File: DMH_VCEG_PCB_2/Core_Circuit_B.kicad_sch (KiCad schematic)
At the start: 103 parts, among them J24 Conn_01x06_PinHeader, J25 Conn_01x10_PinHeader, J26 Conn_01x10_PinHeader, Q17 BC558, Q18 BC558, Q19 BC548, Q20 BC548, Q21 MMBFJ113, Q22 MMBFJ113, Q23 BC548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

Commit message: Synced changes to PCB 2
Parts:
- removed Q21, Q22: MMBFJ113, Package_TO_SOT_THT:TO-92L_Inline, symbol Transistor_FET:MMBFJ113
- removed R108, R115, R116: 100k, Resistor_THT:R_Axial_DIN0207_L6.3mm_D2.5mm_P7.62mm_Horizontal, symbol Device:R_US
- added C75, C76: 100nF, Capacitor_THT:C_Rect_L7.0mm_W4.5mm_P5.00mm, symbol Device:C
- added Q21, Q22: BS170, Package_TO_SOT_THT:TO-92_Inline, symbol Transistor_FET:BS170
- added R19: 47k, Resistor_THT:R_Axial_DIN0207_L6.3mm_D2.5mm_P7.62mm_Horizontal, symbol Device:R_US
- added R199: 100R, Resistor_THT:R_Axial_DIN0207_L6.3mm_D2.5mm_P7.62mm_Horizontal, symbol Device:R_US
- added unit 4 of U13
- R129: value 100k -> 51k
- R131: value 100k -> 47k
- SW4: value DPDT_OnOn -> DPDT_OnOffOn; Function Long B -> Slow B
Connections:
- net -12V: no longer R138.1
- net GND: now also SW4.2 (B), SW4.5 (B), C75.1, C76.1, R19.1; no longer C61.1, C66.2, SW4.3 (C), SW4.6 (C)
- net InvGate: now also Q22.2 (G)
- net Max Level: now also R199.2; no longer U15.9 (-)
- net ProcGate: now also C62.1, D22.1 (K), D24.1 (K), J24.5 (Pin_5), R121.2, SW5.3 (C), U13.1, Q21.2 (G); no longer C64.2, D24.2 (A), R120.1, U11.1
- net at C61.2, C65.1, J25.6 (Pin_6)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: now also C76.2, Q21.1 (D), Q22.1 (D)
- net at C65.2: now also SW4.6 (C); no longer SW4.5 (B)
- net at Q20.1 (C): now also Q22.3 (S)
- net at R134.1, U11.8: now also U15.2 (-); no longer U15.3 (+)
- net at Q18.1 (C): now also Q21.3 (S)
- net at C66.1, C67.1, J25.7 (Pin_7)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: now also C75.2
- net at J24.4 (Pin_4), SW5.2 (B): now also D32.1 (K); no longer R131.1, U11.14
- net at D34.2 (A), U15.1: now also R138.2
- net Inv Sus State: now reaches U16.2, U16.4
- net at U16.10: now also U16.6; no longer D35.2 (A)
- net at U16.9: now also U13.8; no longer U13.4
- net at SW4.4 (A): now also C61.1
- net at SW4.1 (A): now also C66.2
- net at C67.2: now also SW4.3 (C); no longer SW4.2 (B)
- net at C71.2, R143.1: now also U13.9; no longer U16.6
- net Sus State renamed Sus_State
- new net: D32.2 (A), R131.1, U11.14
- new net: R19.2, R199.1, U15.9 (-)
- new net: C64.2, D24.2 (A), R120.1, U11.1
- new net: R138.1, R141.1, U15.3 (+)
- new net: D35.2 (A), U13.4
- no-connect marks 4 -> 2
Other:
- moved on the sheet: C61, C65, C66, C67, C69, C71, C72, D32, D34, D35, J24E, J26J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

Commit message: PCB 2 comp placement ongoing
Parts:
- C75, C76: footprint Capacitor_THT:C_Rect_L7.0mm_W4.5mm_P5.00mm -> Capacitor_THT:C_Disc_D4.3mm_W1.9mm_P5.00mm
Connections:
- net at C65.2: now also SW4.4 (A); no longer SW4.6 (C)
- net at C66.2: now also SW4.3 (C); no longer SW4.1 (A)
- net at C61.1: now also SW4.6 (C); no longer SW4.4 (A)
- net at C67.2: now also SW4.1 (A); no longer SW4.3 (C)
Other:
- moved on the sheet: C61, C65, C66, C67
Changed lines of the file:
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@@
 	(symbol
 		(lib_id "Device:C_Polarized")
-		(at 246.38 97.79 90)
+		(at 246.38 87.63 90)
 		(unit 1)
 		(exclude_from_sim no)
@@
 		(dnp no)
 		(property "Reference" "C65"
-			(at 245.618 91.186 90)
+			(at 245.618 81.026 90)
 			(effects
 				(font
@@
 		)
 		(property "Value" "10uF"
-			(at 245.618 93.726 90)
+			(at 245.618 83.566 90)
 			(effects
 				(font
@@
 		)
 		(property "Footprint" "Capacitor_THT:CP_Radial_D4.0mm_P1.50mm"
-			(at 250.19 96.8248 0)
+			(at 250.19 86.6648 0)
 			(effects
 				(font
@@
 		)
 		(property "Datasheet" "~"
-			(at 246.38 97.79 0)
+			(at 246.38 87.63 0)
 			(effects
 				(font
@@
 		)
 		(property "Description" "Polarized capacitor"
-			(at 246.38 97.79 0)
+			(at 246.38 87.63 0)
 			(effects
 				(font
@@
 		)
 		(property "Function" ""
-			(at 246.38 97.79 0)
+			(at 246.38 87.63 0)
 			(effects
 				(font
@@
 		)
 		(instances
-			(project "DMH_VCEG_PCB_1"
+			(project "DMH_VCEG_PCB_2"
 				(path "/58f4306d-5387-4983-bb08-41a2313fd315/8d22a13f-1d3b-4a1f-8b3f-baf42965c019"
 					(reference "C65")
@@
 		(exclude_from_sim no)
 		(in_bom yes)
-		(on_board yes)
+		(on_board no)
 		(dnp no)
 		(property "Reference" "R199"
@@
 		(exclude_from_sim no)
 		(in_bom yes)
-		(on_board yes)
+		(on_board no)
 		(dnp no)
 		(property "Reference" "R19"
@@
 			)
 		)
-		(property "Footprint" "Capacitor_THT:C_Rect_L7.0mm_W4.5mm_P5.00mm"
+		(property "Footprint" "Capacitor_THT:C_Disc_D4.3mm_W1.9mm_P5.00mm"
 			(at 242.57 76.5048 0)
 			(effects
@@
 	(symbol
 		(lib_id "Device:C")
-		(at 260.35 115.57 90)
+		(at 260.35 125.73 90)
 		(unit 1)
 		(exclude_from_sim no)
@@
 		(dnp no)
 		(property "Reference" "C66"
-			(at 260.35 108.966 90)
+			(at 260.35 119.126 90)
 			(effects
 				(font
@@
 		)
 		(property "Value" "1uF"
-			(at 260.35 111.506 90)
+			(at 260.35 121.666 90)
 			(effects
 				(font
@@
 		)
 		(property "Footprint" "Capacitor_THT:C_Rect_L7.0mm_W4.5mm_P5.00mm"
-			(at 264.16 114.6048 0)
+			(at 264.16 124.7648 0)
 			(effects
 				(font
@@
 		)
 		(property "Datasheet" "~"
-			(at 260.35 115.57 0)
+			(at 260.35 125.73 0)
 			(effects
 				(font
@@
 		)
 		(property "Description" "Unpolarized capacitor"
-			(at 260.35 115.57 0)
+			(at 260.35 125.73 0)
 			(effects
 				(font
@@
 		)
 		(property "Function" "Main Cap B"
-			(at 267.716 117.094 90)
+			(at 267.716 127.254 90)
 			(effects
 				(font
@@
 		)
 		(instances
-			(project "DMH_VCEG_PCB_1"
+			(project "DMH_VCEG_PCB_2"
 				(path "/58f4306d-5387-4983-bb08-41a2313fd315/8d22a13f-1d3b-4a1f-8b3f-baf42965c019"
 					(reference "C66")
@@
 	(symbol
 		(lib_id "Device:C")
-		(at 246.38 87.63 270)
+		(at 246.38 97.79 270)
 		(mirror x)
 		(unit 1)
@@
 		(dnp no)
 		(property "Reference" "C61"
-			(at 246.253 81.026 90)
+			(at 246.253 91.186 90)
 			(effects
 				(font
@@
 		)
 		(property "Value" "1uF"
-			(at 246.253 83.566 90)
+			(at 246.253 93.726 90)
 			(effects
 				(font
@@
 		)
 		(property "Footprint" "Capacitor_THT:C_Rect_L7.0mm_W4.5mm_P5.00mm"
-			(at 242.57 86.6648 0)
+			(at 242.57 96.8248 0)
 			(effects
 				(font
@@
 		)
 		(property "Datasheet" "~"
-			(at 246.38 87.63 0)
+			(at 246.38 97.79 0)
 			(effects
 				(font
@@
 		)
 		(property "Description" "Unpolarized capacitor"
-			(at 246.38 87.63 0)
+			(at 246.38 97.79 0)
 			(effects
 				(font
@@
 		)
 		(property "Function" ""
-			(at 246.38 87.63 0)
+			(at 246.38 97.79 0)
 			(effects
 				(font
@@
 		)
 		(instances
-			(project "DMH_VCEG_PCB_1"
+			(project "DMH_VCEG_PCB_2"
 				(path "/58f4306d-5387-4983-bb08-41a2313fd315/8d22a13f-1d3b-4a1f-8b3f-baf42965c019"
 					(reference "C61")
@@
 			)
 		)
-		(property "Footprint" "Capacitor_THT:C_Rect_L7.0mm_W4.5mm_P5.00mm"
+		(property "Footprint" "Capacitor_THT:C_Disc_D4.3mm_W1.9mm_P5.00mm"
 			(at 256.54 104.4448 0)
 			(effects
@@
 	(symbol
 		(lib_id "Device:C_Polarized")
-		(at 260.35 125.73 90)
+		(at 260.35 115.57 90)
 		(unit 1)
 		(exclude_from_sim no)
@@
 		(dnp no)
 		(property "Reference" "C67"
-			(at 260.35 119.126 90)
+			(at 260.35 108.966 90)
 			(effects
 				(font
@@
 		)
 		(property "Value" "10uF"
-			(at 260.35 121.666 90)
+			(at 260.35 111.506 90)
 			(effects
 				(font
@@
 		)
 		(property "Footprint" "Capacitor_THT:CP_Radial_D4.0mm_P1.50mm"
-			(at 264.16 124.7648 0)
+			(at 264.16 114.6048 0)
 			(effects
 				(font
@@
 		)
 		(property "Datasheet" "~"
-			(at 260.35 125.73 0)
+			(at 260.35 115.57 0)
 			(effects
 				(font
@@
 		)
 		(property "Description" "Polarized capacitor"
-			(at 260.35 125.73 0)
+			(at 260.35 115.57 0)
 			(effects
 				(font
@@
 		)
 		(property "Function" ""
-			(at 260.35 125.73 0)
+			(at 260.35 115.57 0)
 			(effects
 				(font
@@
 		)
 		(instances
-			(project "DMH_VCEG_PCB_1"
+			(project "DMH_VCEG_PCB_2"
 				(path "/58f4306d-5387-4983-bb08-41a2313fd315/8d22a13f-1d3b-4a1f-8b3f-baf42965c019"
 					(reference "C67")

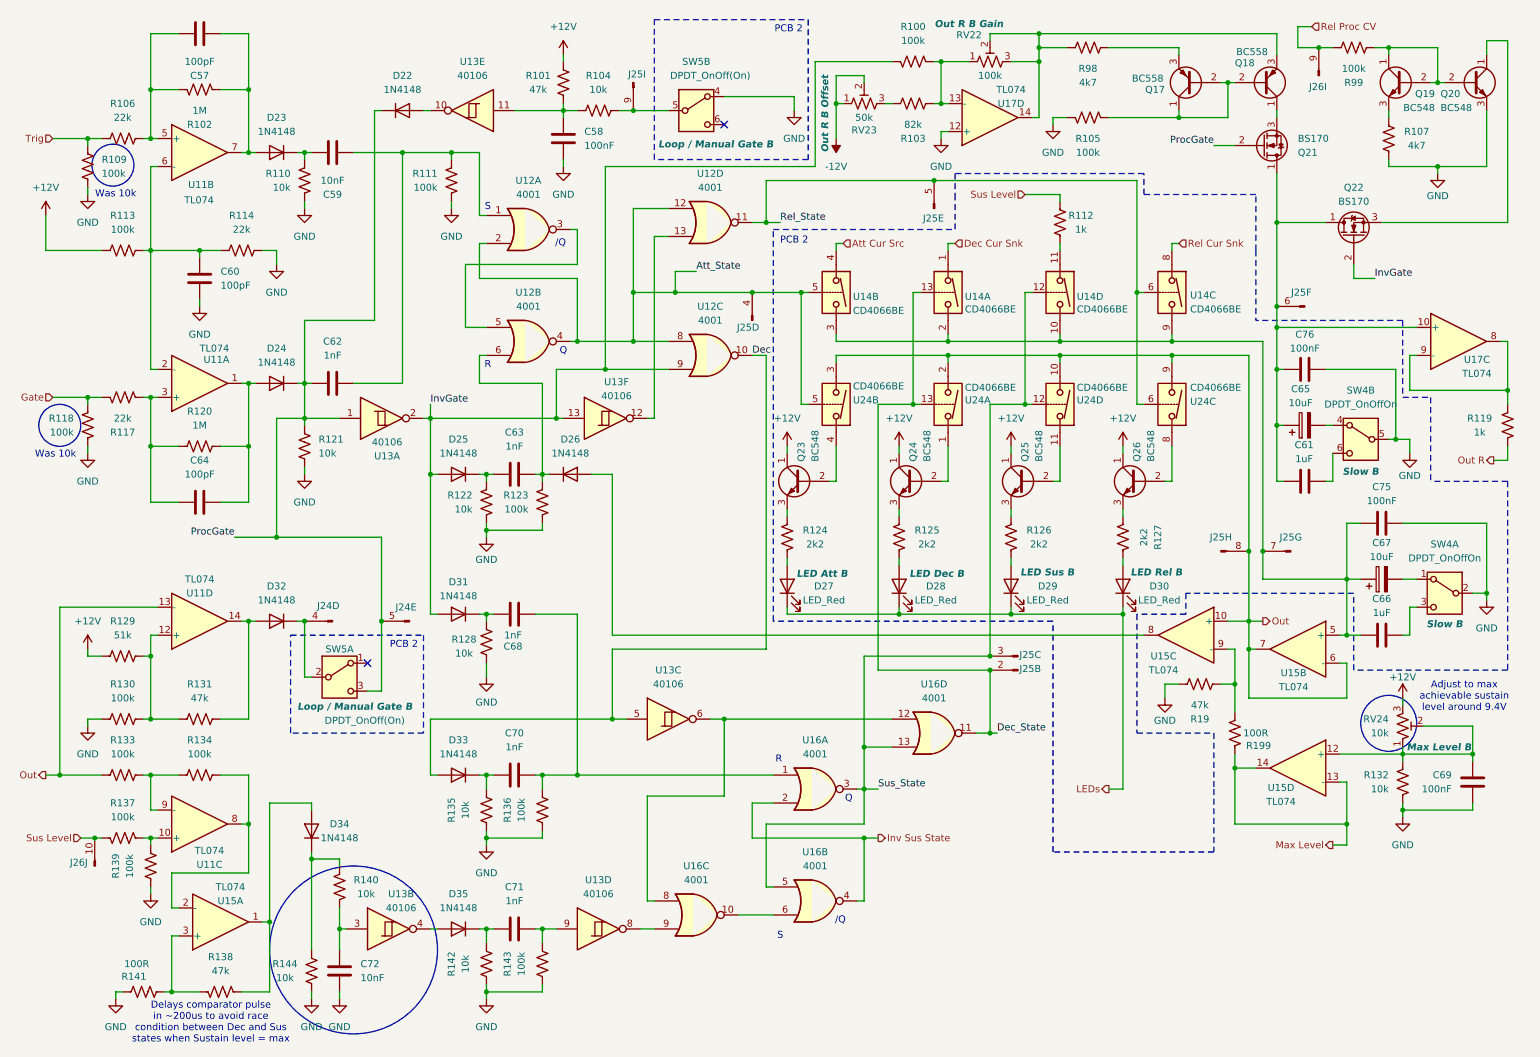
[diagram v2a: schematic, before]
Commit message: Synced PCB 1 and 2
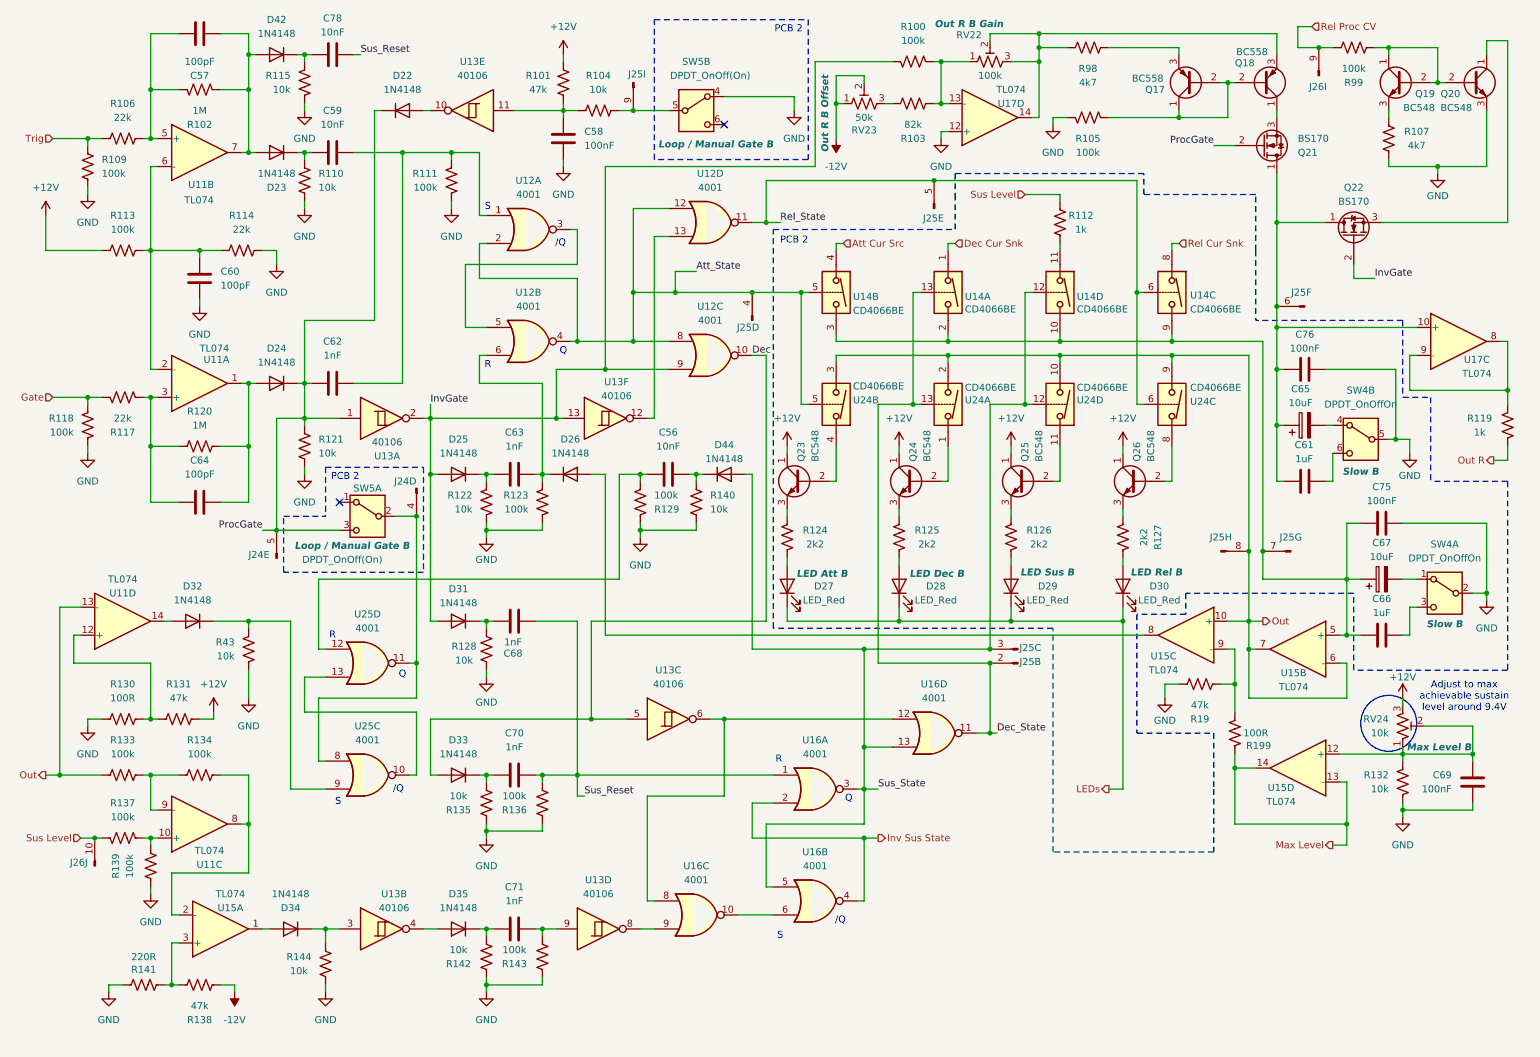
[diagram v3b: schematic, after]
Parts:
- removed C72: 10nF, Capacitor_THT:C_Disc_D4.3mm_W1.9mm_P5.00mm, symbol Device:C
- added C56, C78: 10nF, Capacitor_THT:C_Disc_D4.3mm_W1.9mm_P5.00mm, symbol Device:C
- added D42, D44: 1N4148, Diode_THT:D_DO-35_SOD27_P7.62mm_Horizontal, symbol Diode:1N4148
- added R115, R43: 10k, Resistor_THT:R_Axial_DIN0207_L6.3mm_D2.5mm_P7.62mm_Horizontal, symbol Device:R_US
- added U25: 4001, Package_DIP:DIP-14_W7.62mm_Socket, symbol 4xxx:4001
- R129: value 51k -> 100k
- R130: value 100k -> 100R
- R141: value 100R -> 220R
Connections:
- net +12V: now also R131.1; no longer R129.2
- net -12V: now also R138.2
- net GND: now also R129.2, R140.1, R115.1, R43.1
- net Sus_State: now also D44.2 (A)
- net at J24.4 (Pin_4), SW5.2 (B): now also U25.11, U25.8; no longer D32.1 (K)
- net at D32.2 (A), U11.14: no longer R131.1
- net at C57.2, D23.2 (A), R102.1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: now also D42.2 (A)
- net Sus_Reset: now reaches C68.2, C70.2, R136.1, U16.1
- net Sus_Reset: now also C78.2
- net at D34.2 (A), U15.1: no longer R138.2
- net at R130.1, R131.2, U11.12 (+): no longer R129.1
- net at D34.1 (K), R144.1: now also U13.3; no longer R140.1
- net at R140.2: now also C56.2, D44.1 (K); no longer U13.3
- new net: D32.1 (K), R43.2, U25.9
- new net: C56.1, R129.1, U25.12
- new net: U25.10, U25.13
- new net: C78.1, D42.1 (K), R115.2
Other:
- note removed: "Delays comparator pulse in ~200us to avoid race condition between Dec and Sus states when Sustain level = max"
- note removed: "Was 10k"
- moved on the sheet: C68, D23, D31, D32, D34, J25B, J25C, R110, R128, R131, R135, R136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

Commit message: Restarted component placing on Main
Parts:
- renumbered J25 to J26, J25 to J27
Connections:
- net Att Cur Src: now also U14.8; no longer U14.4
- net Att_State: now also J25.8 (Pin_8), U14.6, U24.6; no longer J25.4 (Pin_4), U14.5, U24.5
- net Dec Cur Snk: now also U14.11; no longer U14.1
- net Dec_State: now also J25.5 (Pin_5), U14.12, U24.12; no longer J25.2 (Pin_2), U14.13, U24.13
- net Out: now also J26.7 (Pin_7), U24.10, U24.2, U24.3, U24.9; no longer J26.8 (Pin_8), U24.10, U24.2, U24.3, U24.9
- net Rel Cur Snk: now also U14.4; no longer U14.8
- net Rel_State: now also J25.7 (Pin_7), U14.5, U24.5; no longer J25.5 (Pin_5), U14.6, U24.6
- net Sus_State: now also J25.4 (Pin_4), U14.13, U24.13; no longer J25.3 (Pin_3), U14.12, U24.12
- net at Q23.2 (B): now also U24.8; no longer U24.4
- net at C61.2, C65.1, C76.2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: now also J27.10 (Pin_10); no longer J27.6 (Pin_6)
- net at Q25.2 (B): now also U24.1; no longer U24.11
- net at Q26.2 (B): now also U24.4; no longer U24.8
- net at R112.1: now also U14.1; no longer U14.11
- net at Q24.2 (B): now also U24.11; no longer U24.1
- new net: C66.1, C67.1, C75.2, J25.9 (Pin_9), U14.10, U14.2, U14.3, U14.9, U15.5 (+)

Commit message: PCB 2 placement done
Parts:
- D27, D28, D29, D30: value LED_Red -> LED_R
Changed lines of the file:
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@@
 			)
 		)
-		(property "Value" "LED_Red"
+		(property "Value" "LED_R"
 			(at 219.964 119.38 90)
 			(effects
@@
 			)
 		)
-		(property "Value" "LED_Red"
+		(property "Value" "LED_R"
 			(at 199.7075 119.38 90)
 			(effects
@@
 			)
 		)
-		(property "Value" "LED_Red"
+		(property "Value" "LED_R"
 			(at 179.3875 119.38 90)
 			(effects
@@
 			)
 		)
-		(property "Value" "LED_Red"
+		(property "Value" "LED_R"
 			(at 159.0675 119.38 90)
 			(effects

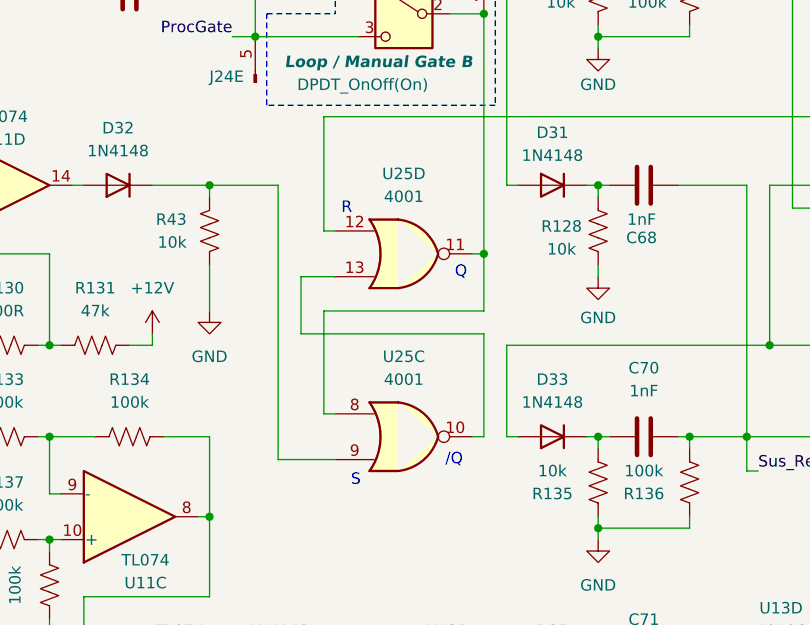
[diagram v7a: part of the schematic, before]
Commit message: PCB 1 placement in progress
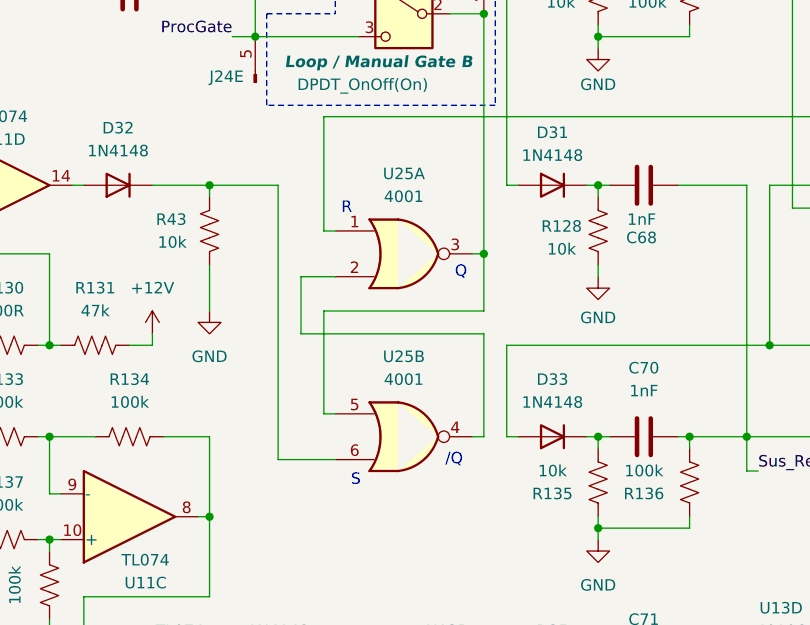
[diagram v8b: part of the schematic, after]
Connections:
- net at D32.1 (K), R43.2: now also U25.6; no longer U25.9
- net at J24.4 (Pin_4), SW5.2 (B): now also U25.3, U25.5; no longer U25.11, U25.8
- net at C56.1, R129.1: now also U25.1; no longer U25.12
- new net: U25.2, U25.4
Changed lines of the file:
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@@
 		(lib_id "4xxx:4001")
 		(at 76.2 130.81 0)
-		(unit 4)
+		(unit 1)
 		(exclude_from_sim no)
 		(in_bom yes)
@@
 				(path "/58f4306d-5387-4983-bb08-41a2313fd315/8d22a13f-1d3b-4a1f-8b3f-baf42965c019"
 					(reference "U25")
-					(unit 4)
+					(unit 1)
 				)
 			)
@@
 		(lib_id "4xxx:4001")
 		(at 76.2 151.13 0)
-		(unit 3)
+		(unit 2)
 		(exclude_from_sim no)
 		(in_bom yes)
@@
 				(path "/58f4306d-5387-4983-bb08-41a2313fd315/8d22a13f-1d3b-4a1f-8b3f-baf42965c019"
 					(reference "U25")
-					(unit 3)
+					(unit 2)
 				)
 			)
